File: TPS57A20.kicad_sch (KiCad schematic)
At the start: 3 parts, among them U4 TPS7A20xxxDQN

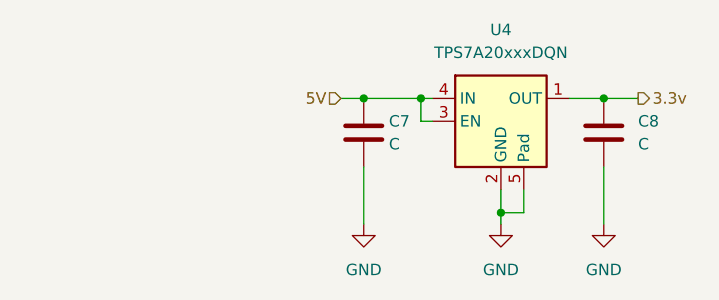
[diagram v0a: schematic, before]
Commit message: incomplete calcs for TPS
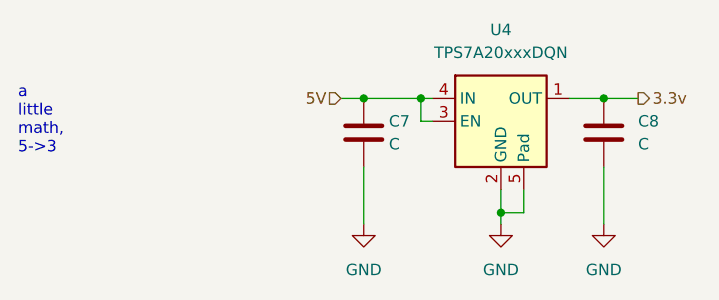
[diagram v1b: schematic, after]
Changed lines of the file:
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@@
 	(generator_version "9.0")
 	(paper "A4")
+	(text_box "a little math, 5->3"
+		(exclude_from_sim no)
+		(at 74.93 99.06 0)
+		(size 0 0)
+		(margins 0.9525 0.9525 0.9525 0.9525)
+		(stroke
+			(width 0)
+			(type solid)
+		)
+		(fill
+			(type none)
+		)
+		(effects
+			(font
+				(size 1.27 1.27)
+			)
+			(justify left top)
+		)
+	)
 	(junction
 		(at 114.3 101.6)

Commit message: finished math
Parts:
- C7, C8: value C -> 1u
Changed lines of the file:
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@@
 	(generator_version "9.0")
 	(paper "A4")
-	(text_box "a little math, 5->3"
-		(exclude_from_sim no)
-		(at 74.93 99.06 0)
-		(size 0 0)
-		(margins 0.9525 0.9525 0.9525 0.9525)
-		(stroke
-			(width 0)
-			(type solid)
-		)
-		(fill
-			(type none)
-		)
-		(effects
-			(font
-				(size 1.27 1.27)
-			)
-			(justify left top)
-		)
-	)
 	(junction
 		(at 114.3 101.6)
@@
 			)
 		)
-		(property "Value" "C"
+		(property "Value" "1u"
 			(at 117.094 106.68 0)
 			(effects
@@
 			)
 		)
-		(property "Value" "C"
+		(property "Value" "1u"
 			(at 144.78 106.6799 0)
 			(effects

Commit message: added secondary circuit
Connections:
- net 3.3v renamed +3.3V
- net 5V renamed +5V
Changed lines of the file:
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@@
-		)
-	)
-	(hierarchical_label "5V"
-		(shape input)
-		(at 111.76 101.6 180)
-		(effects
-			(font
-				(size 1.27 1.27)
-			)
-			(justify right)
-		)
-	)
-	(hierarchical_label "3.3v"
-		(shape output)
-		(at 144.78 101.6 0)
-		(effects
-			(font
-				(size 1.27 1.27)
-			)
-			(justify left)
 		)
 	)
@@
 				(path "/f2987657-b7e0-480f-b307-23af9e47acd8/b1bb47a3-165c-4c9a-9065-ca3b3c01af3d"
 					(reference "C7")
+					(unit 1)
+				)
+			)
+		)
+	)
+	(symbol
+		(lib_id "power:+3.3V")
+		(at 144.78 101.6 270)
+		(unit 1)
+		(exclude_from_sim no)
+		(in_bom yes)
+		(on_board yes)
+		(dnp no)
+		(fields_autoplaced yes)
+		(property "Reference" "#PWR021"
+			(at 140.97 101.6 0)
+			(effects
+				(font
+					(size 1.27 1.27)
+				)
+				(hide yes)
+			)
+		)
+		(property "Value" "+3.3V"
+			(at 149.86 101.6 0)
+			(effects
+				(font
+					(size 1.27 1.27)
+				)
+			)
+		)
+		(property "Footprint" ""
+			(at 144.78 101.6 0)
+			(effects
+				(font
+					(size 1.27 1.27)
+				)
+				(hide yes)
+			)
+		)
+		(property "Datasheet" ""
+			(at 144.78 101.6 0)
+			(effects
+				(font
+					(size 1.27 1.27)
+				)
+				(hide yes)
+			)
+		)
+		(property "Description" "Power symbol creates a global label with name \"+3.3V\""
+			(at 144.78 101.6 0)
+			(effects
+				(font
+					(size 1.27 1.27)
+				)
+				(hide yes)
+			)
+		)
+		(pin "1"
+		)
+		(instances
+			(project ""
+				(path "/f2987657-b7e0-480f-b307-23af9e47acd8/b1bb47a3-165c-4c9a-9065-ca3b3c01af3d"
+					(reference "#PWR021")
 					(unit 1)
 				)
@@
 					(unit 1)
 				)
+			)
+		)
+	)
+	(symbol
+		(lib_id "power:+5V")
+		(at 111.76 101.6 90)
+		(unit 1)
+		(exclude_from_sim no)
+		(in_bom yes)
+		(on_board yes)
+		(dnp no)
+		(fields_autoplaced yes)
+		(property "Reference" "#PWR020"
+			(at 115.57 101.6 0)
+			(effects
+				(font
+					(size 1.27 1.27)
+				)
+				(hide yes)
+			)
+		)
+		(property "Value" "+5V"
+			(at 106.68 101.6 0)
+			(effects
+				(font
+					(size 1.27 1.27)
+				)
+			)
+		)
+		(property "Footprint" ""
+			(at 111.76 101.6 0)
+			(effects
+				(font
+					(size 1.27 1.27)
+				)
+				(hide yes)
+			)
+		)
+		(property "Datasheet" ""
+			(at 111.76 101.6 0)
+			(effects
+				(font
+					(size 1.27 1.27)
+				)
+				(hide yes)
+			)
+		)
+		(property "Description" "Power symbol creates a global label with name \"+5V\""
+			(at 111.76 101.6 0)
+			(effects
+				(font
+					(size 1.27 1.27)
+				)
+				(hide yes)
+			)
+		)
+		(pin "1"
+		)
+		(instances
+			(project ""
+				(path "/f2987657-b7e0-480f-b307-23af9e47acd8/b1bb47a3-165c-4c9a-9065-ca3b3c01af3d"
+					(reference "#PWR020")
+					(unit 1)
+				)
